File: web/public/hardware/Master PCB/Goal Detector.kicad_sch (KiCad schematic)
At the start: 14 parts, among them U4 LM339

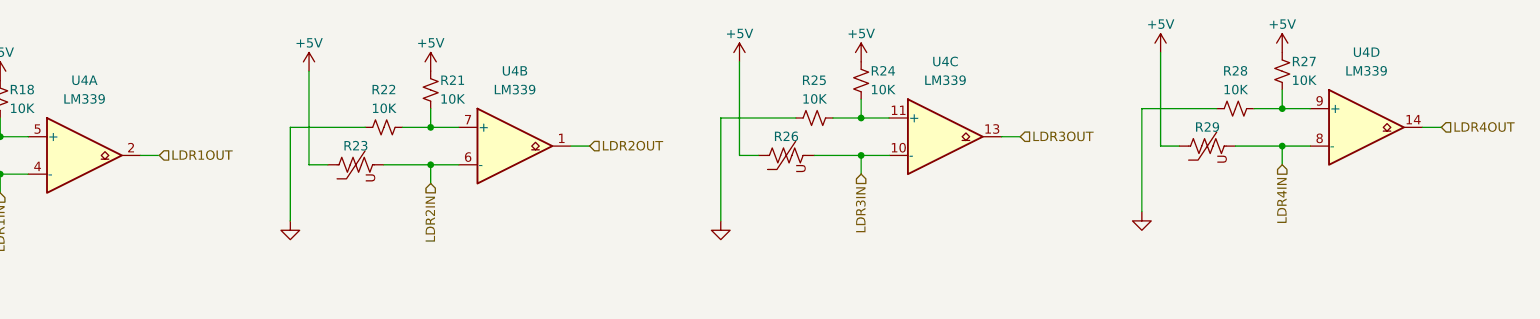
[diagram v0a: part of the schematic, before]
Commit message: Add goal detection pull-up resistors
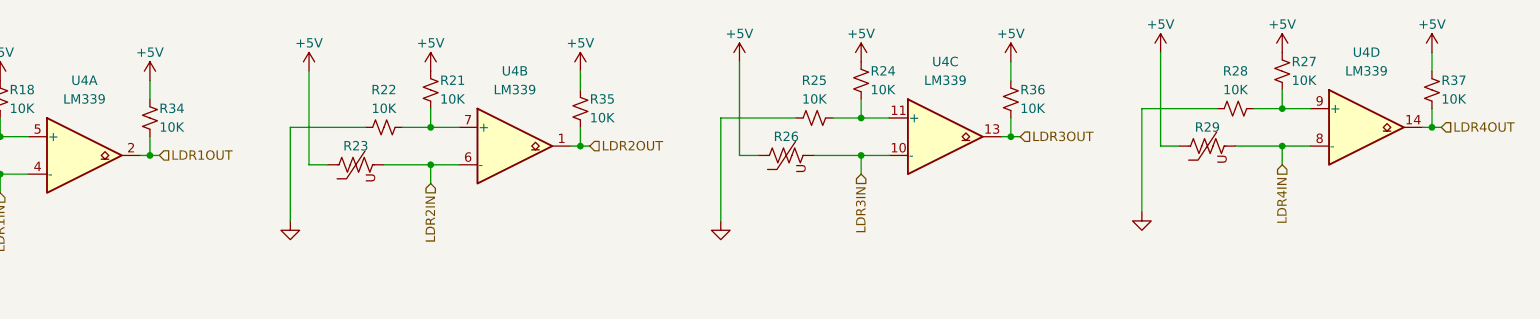
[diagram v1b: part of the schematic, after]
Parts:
- added R34, R35, R36, R37: 10K, symbol Device:R_Small_US
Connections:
- net +5V: now also R34.1, R35.1, R36.1, R37.1
- net LDR1OUT: now also R34.2
- net LDR2OUT: now also R35.2
- net LDR3OUT: now also R36.2
- net LDR4OUT: now also R37.2

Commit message: Finish schematic and start routing PCB
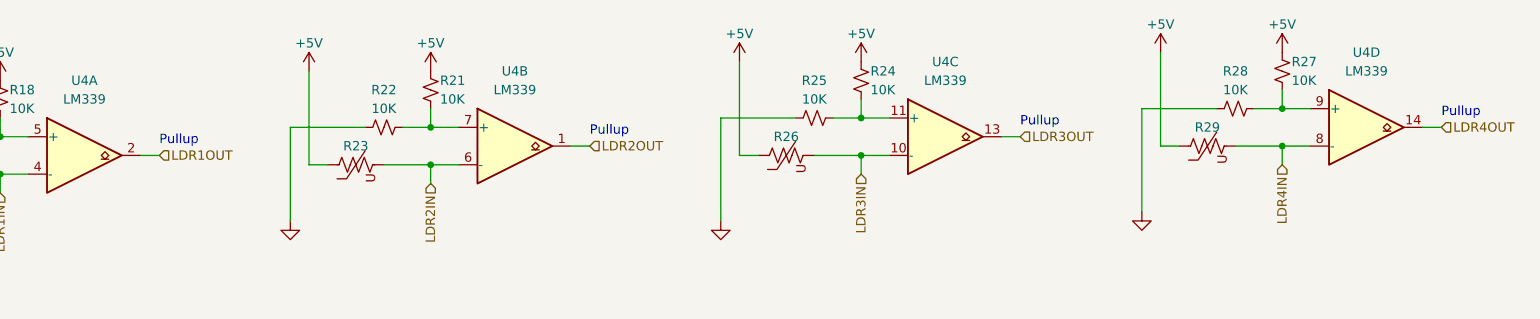
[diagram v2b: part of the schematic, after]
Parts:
- removed R34, R35, R36, R37: 10K, symbol Device:R_Small_US
- C20: footprint (none) -> Capacitor_SMD:C_0805_2012Metric_Pad1.18x1.45mm_HandSolder
- R18, R19, R20, R21, R22, R23, R24, R25, R26, R27, R28, R29: footprint (none) -> Resistor_SMD:R_0805_2012Metric_Pad1.20x1.40mm_HandSolder
- U4: footprint (none) -> Package_DIP:DIP-14_W7.62mm_LongPads
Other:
- note added: "Pullup"

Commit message: Route lots
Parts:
- U4: footprint Package_DIP:DIP-14_W7.62mm_LongPads -> Package_SO:TSSOP-14_4.4x5mm_P0.65mm
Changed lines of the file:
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@@
       (effects (font (size 1.27 1.27)))
     )
-    (property "Footprint" "Package_DIP:DIP-14_W7.62mm_LongPads" (at 115.57 74.93 0)
+    (property "Footprint" "Package_SO:TSSOP-14_4.4x5mm_P0.65mm" (at 115.57 74.93 0)
       (effects (font (size 1.27 1.27)) hide)
     )
@@
       (effects (font (size 1.27 1.27)) (justify left))
     )
-    (property "Footprint" "Package_DIP:DIP-14_W7.62mm_LongPads" (at 129.54 114.3 0)
+    (property "Footprint" "Package_SO:TSSOP-14_4.4x5mm_P0.65mm" (at 129.54 114.3 0)
       (effects (font (size 1.27 1.27)) hide)
     )
@@
       (effects (font (size 1.27 1.27)))
     )
-    (property "Footprint" "Package_DIP:DIP-14_W7.62mm_LongPads" (at 173.99 73.66 0)
+    (property "Footprint" "Package_SO:TSSOP-14_4.4x5mm_P0.65mm" (at 173.99 73.66 0)
       (effects (font (size 1.27 1.27)) hide)
     )
@@
       (effects (font (size 1.27 1.27)))
     )
-    (property "Footprint" "Package_DIP:DIP-14_W7.62mm_LongPads" (at 57.15 76.2 0)
+    (property "Footprint" "Package_SO:TSSOP-14_4.4x5mm_P0.65mm" (at 57.15 76.2 0)
       (effects (font (size 1.27 1.27)) hide)
     )
@@
       (effects (font (size 1.27 1.27)))
     )
-    (property "Footprint" "Package_DIP:DIP-14_W7.62mm_LongPads" (at 231.14 72.39 0)
-      (effects (font (size 1.27 1.27)) hide)
-    )
+    (property "Footprint" "Package_SO:TSSOP-14_4.4x5mm_P0.65mm" (at 231.14 72.39 0)
+      (effects (font (size 1.27 1.27)) hide)
+    )

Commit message: Change STM32 pinout, begin placing components on new PCB
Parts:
- removed R20, R23, R26, R29: 10K, Resistor_SMD:R_0805_2012Metric_Pad1.20x1.40mm_HandSolder, symbol Device:Varistor_US
- added RV1, RV2, RV3, RV4: 10K, symbol Device:R_Potentiometer_Trim_US
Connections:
- net +5V: now also RV1.3, RV2.3, RV3.3, RV4.3
- net LDR1IN: now also RV1.2
- net LDR2IN: now also RV2.2
- net LDR3IN: now also RV3.2
- net LDR4IN: now also RV4.2
- no-connect marks 0 -> 4

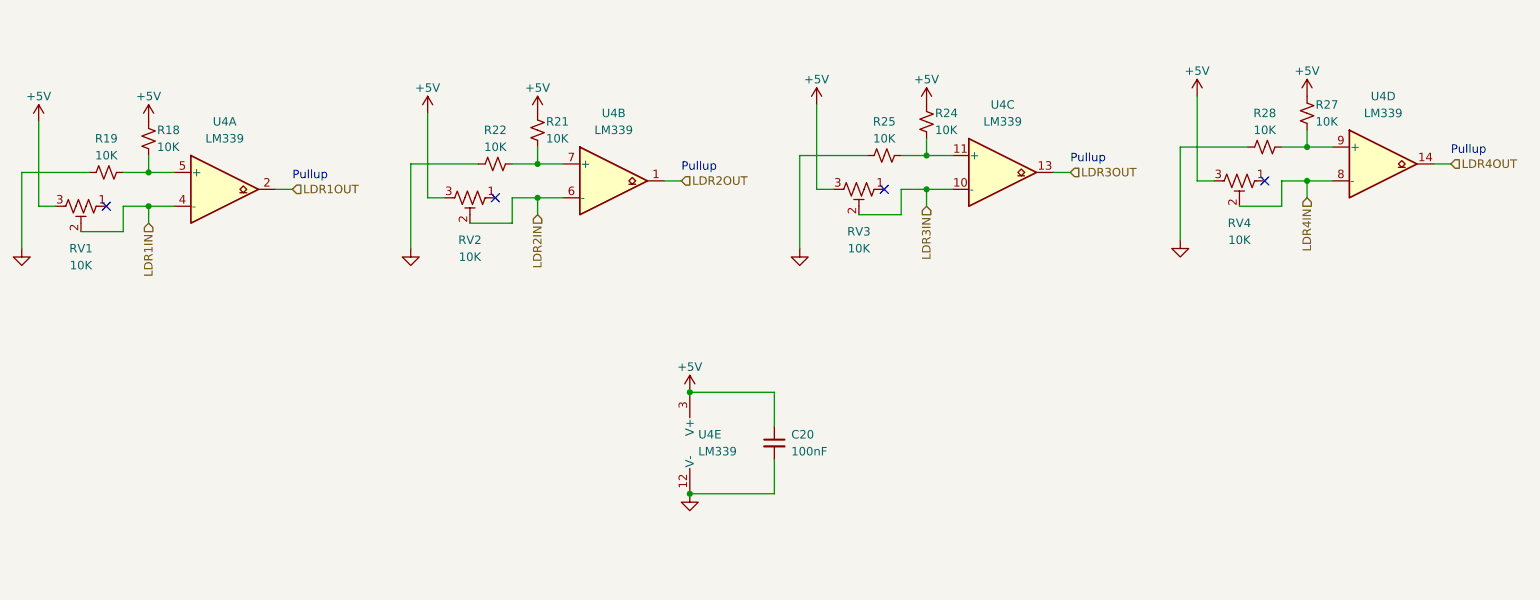
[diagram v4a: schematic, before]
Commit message: Add ESD ICs and route part of board
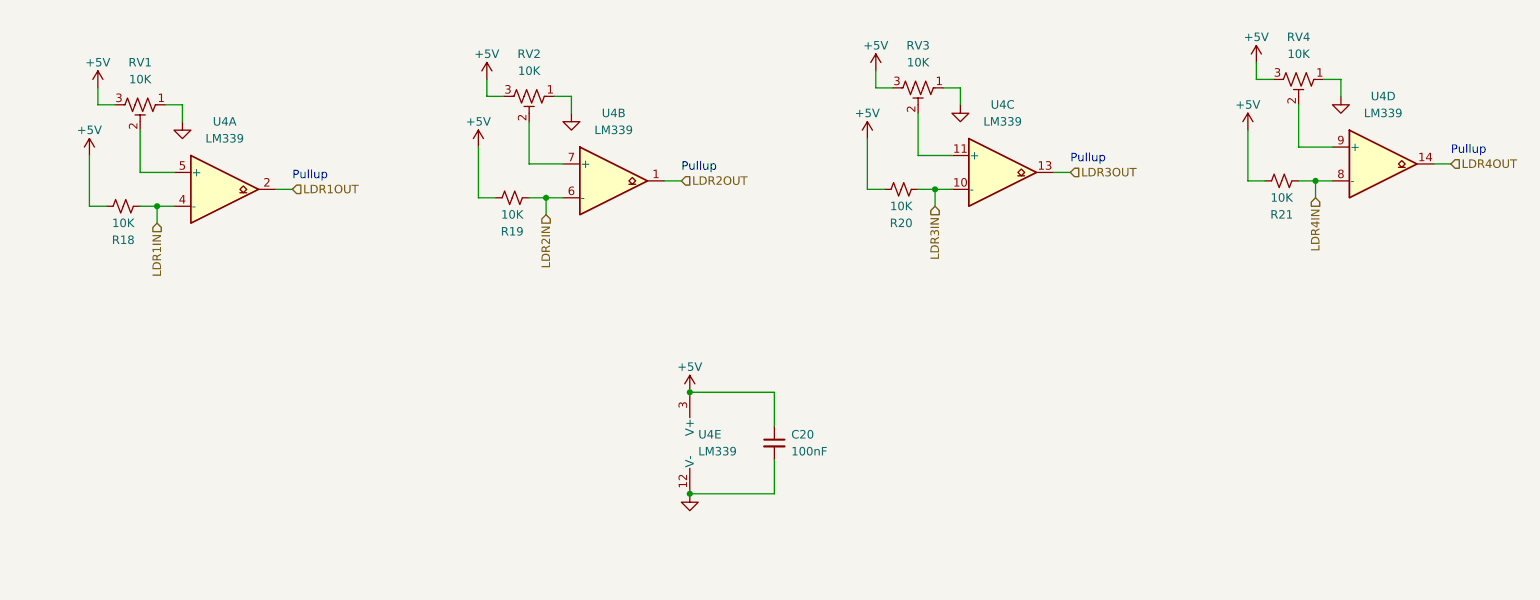
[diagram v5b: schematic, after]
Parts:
- removed R22, R24, R25, R27, R28: 10K, Resistor_SMD:R_0805_2012Metric_Pad1.20x1.40mm_HandSolder, symbol Device:R_Small_US
- added R20: 10K, Resistor_SMD:R_0805_2012Metric_Pad1.20x1.40mm_HandSolder, symbol Device:R_Small_US
- RV1, RV2, RV3, RV4: footprint (none) -> Potentiometer_SMD:Potentiometer_Bourns_TC33X_Vertical
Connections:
- net +5V: now also R18.2, R19.2, R21.2, R20.2; no longer R18.1, R21.1
- net GND: now also RV1.1, RV2.1, RV3.1, RV4.1; no longer R19.1
- net LDR1IN: now also R18.1; no longer RV1.2
- net LDR2IN: now also R19.1; no longer RV2.2
- net LDR3IN: now also R20.1; no longer RV3.2
- net LDR4IN: now also R21.1; no longer RV4.2
- net at U4.7 (+): now also RV2.2; no longer R21.2
- net at U4.9 (+): now also RV4.2
- net at U4.11 (+): now also RV3.2
- new net: RV1.2, U4.5 (+)
- no-connect marks 4 -> 0

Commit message: Finish routing
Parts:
- RV1, RV2, RV3, RV4: footprint Potentiometer_SMD:Potentiometer_Bourns_TC33X_Vertical -> Potentiometer_THT:Potentiometer_Bourns_3296W_Vertical
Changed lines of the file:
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@@
       (effects (font (size 1.27 1.27)))
     )
-    (property "Footprint" "Potentiometer_SMD:Potentiometer_Bourns_TC33X_Vertical" (at 104.14 64.77 0)
+    (property "Footprint" "Potentiometer_THT:Potentiometer_Bourns_3296W_Vertical" (at 104.14 64.77 0)
       (effects (font (size 1.27 1.27)) hide)
     )
@@
       (effects (font (size 1.27 1.27)))
     )
-    (property "Footprint" "Potentiometer_SMD:Potentiometer_Bourns_TC33X_Vertical" (at 219.71 62.23 0)
+    (property "Footprint" "Potentiometer_THT:Potentiometer_Bourns_3296W_Vertical" (at 219.71 62.23 0)
       (effects (font (size 1.27 1.27)) hide)
     )
@@
       (effects (font (size 1.27 1.27)))
     )
-    (property "Footprint" "Potentiometer_SMD:Potentiometer_Bourns_TC33X_Vertical" (at 162.56 63.5 0)
+    (property "Footprint" "Potentiometer_THT:Potentiometer_Bourns_3296W_Vertical" (at 162.56 63.5 0)
       (effects (font (size 1.27 1.27)) hide)
     )
@@
       (effects (font (size 1.27 1.27)))
     )
-    (property "Footprint" "Potentiometer_SMD:Potentiometer_Bourns_TC33X_Vertical" (at 45.72 66.04 0)
-      (effects (font (size 1.27 1.27)) hide)
-    )
+    (property "Footprint" "Potentiometer_THT:Potentiometer_Bourns_3296W_Vertical" (at 45.72 66.04 0)
+      (effects (font (size 1.27 1.27)) hide)
+    )

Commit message: More misc. cleanup and generate updated production files
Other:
- note added: "Comparator decoupling"
- note added: "LDR comparators"
- moved on the sheet: C20, R18, R19, R20, R21, RV1, RV2, RV3, RV4, U4A, U4B, U4C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
